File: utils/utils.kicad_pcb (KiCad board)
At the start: 2 copper layers, 32.2 x 114.5 mm, 23 parts, among them J1 AIN, J2 BIN, J3 GATE, J4 EURORACK_CONN_16, J5 ~OUT, J6 OUT, J7 Conn_01x04, J8 Conn_01x05, U1 TL072, U2 4066, U3 LM317, U4 LM337

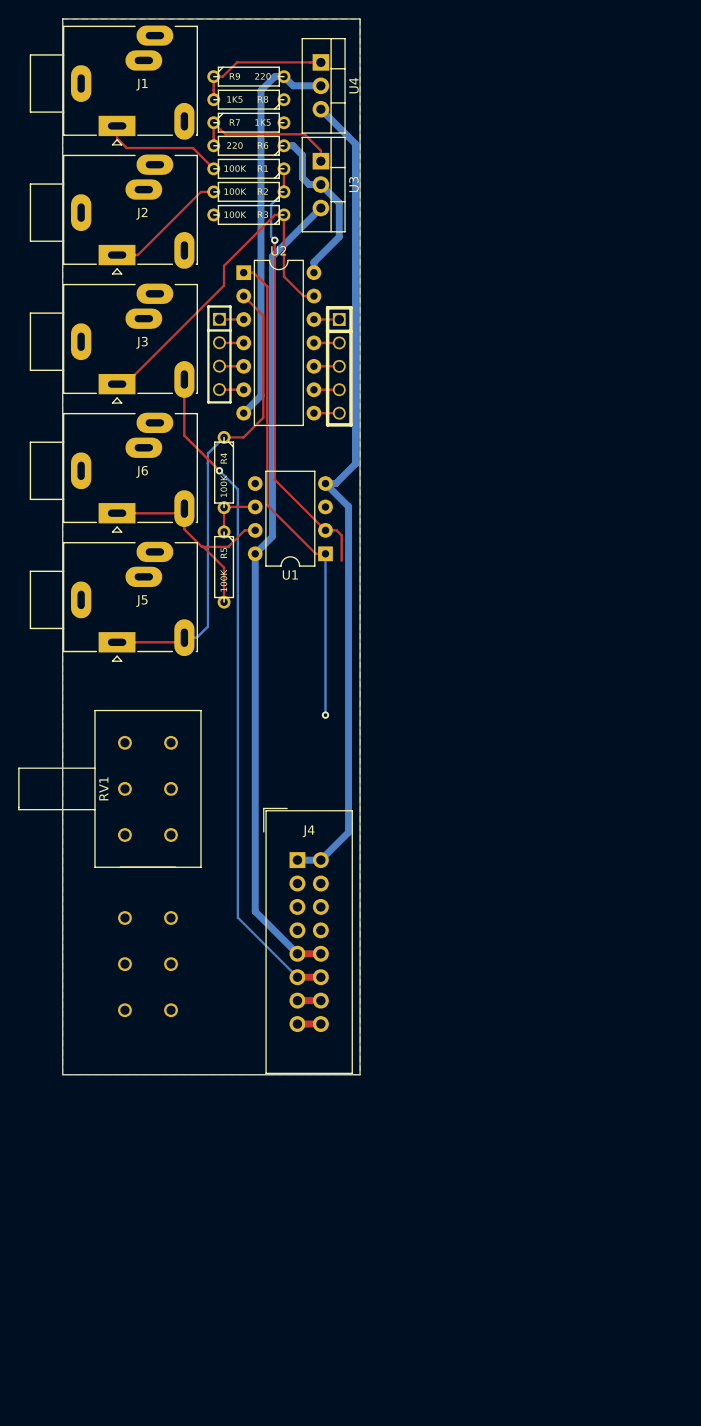
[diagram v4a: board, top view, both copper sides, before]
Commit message: shrunk board
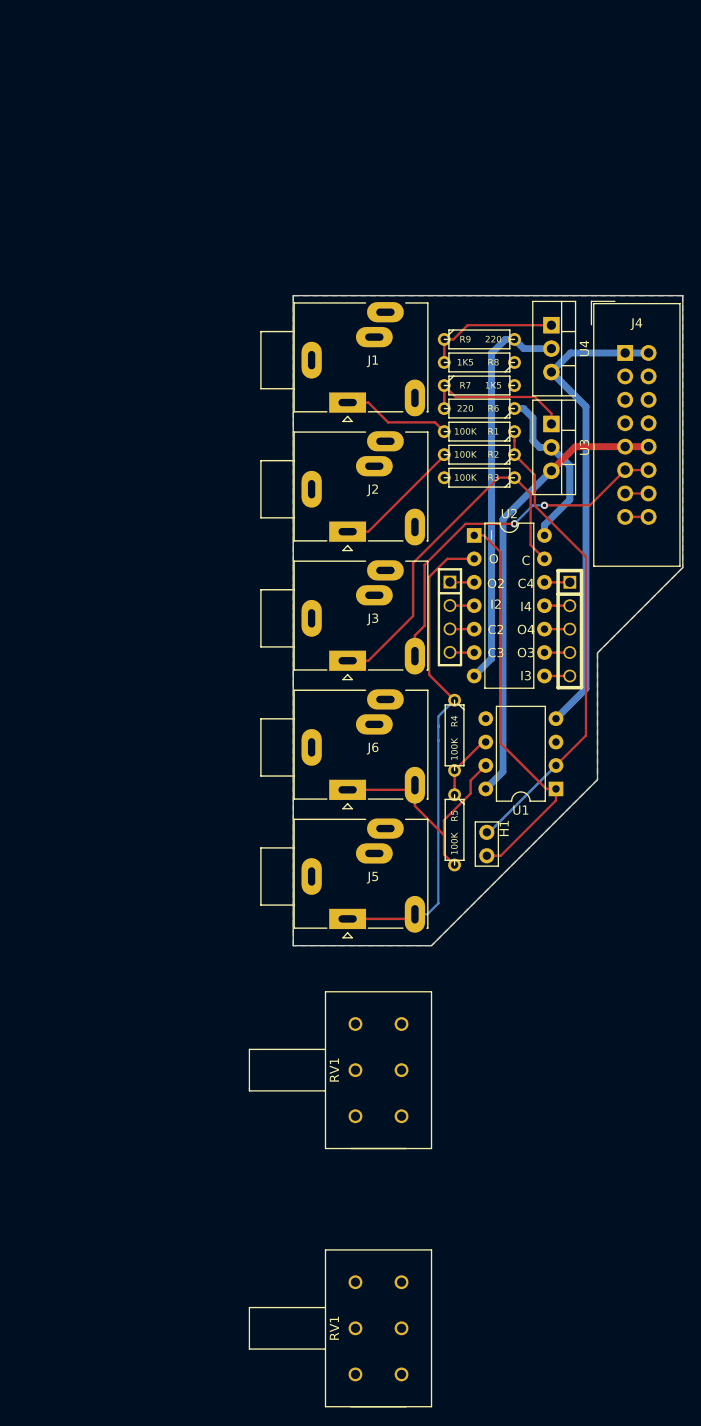
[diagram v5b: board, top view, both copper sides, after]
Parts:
- added H1: ?, 4ms/4ms-kicad-lib/lib-footprints/4ms_Connector.pretty:Pins_1x02_2.54mm_TH, F.Cu at (144.0, 102.5)
- RV1: moved to F.Cu
- moved J4 65.5 mm to (159.0, 49.2)
- moved RV1 46.7 mm to (132.2, 155.0), turned to 270 degrees
- moved RV1 39.4 mm to (132.2, 127.0)
- moved J1 39.1 mm to (128.9, 54.6)
- moved J5 39.1 mm to (128.9, 110.6)
- moved J6 39.1 mm to (128.9, 96.6)
- moved J2 39.1 mm to (128.9, 68.6)
- moved J3 39.1 mm to (128.9, 82.6)
- moved U2 37.9 mm to (142.6, 69.0)
- moved J7 37.9 mm to (140.0, 77.9)
- moved J8 37.9 mm to (153.0, 79.2)
- moved R1 37.9 mm to (143.2, 57.8)
- moved R2 37.9 mm to (143.2, 60.2)
- moved R3 37.9 mm to (143.2, 62.8)
- moved R4 37.9 mm to (140.5, 90.7)
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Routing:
- net +12V: track 88.3 -> 49.1 mm
- net -12V: track 89.8 -> 51.9 mm
- net +5V: track 72.4 -> 38.9 mm
- net Net-(RV1-Pad6): track 52.9 -> 44.0 mm, vias 1 -> 0
- net Net-(R1-Pad1): track 47.0 -> 51.3 mm, vias 1 -> 0
- net GATE: track 37.8 -> 40.7 mm
- net ~OUT: track 51.1 -> 53.6 mm
- net AIN: track 13.2 -> 11.8 mm
- net Net-(R4-Pad2): track 6.45 -> 7.81 mm
- net OUT: track 26.1 -> 27.4 mm
- net BIN: track 13.3 -> 14.0 mm
- added copper zone on B.Cu, net GND
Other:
- board size 32.2 x 114.5 mm -> 42.2 x 70.5 mm
- board text added: "BIGASS | Rev. A | 2020-05-23"
- board text added: "C"
- board text added: "C2"
- board text added: "C3"
- board text added: "C4"
- board text added: "I"
- board text added: "I2"
- board text added: "I3"
- board text added: "I4"
- board text added: "O"
- board text added: "O2"
- board text added: "O3"
- board text added: "O4"
- board text added: "https://rabid.audio"
- board text removed: "TODO: what is standard spacing for knobs?"

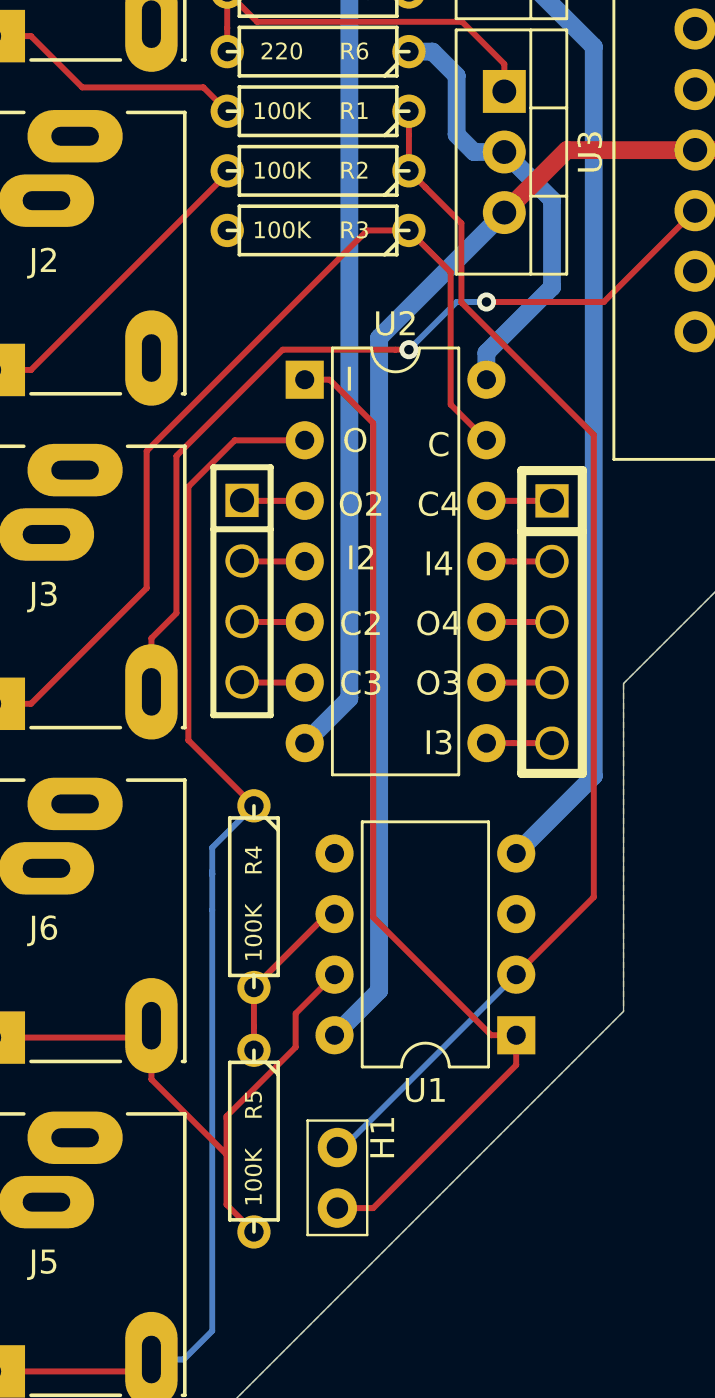
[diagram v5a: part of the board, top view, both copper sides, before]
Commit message: move the quirks of the pcb out of the schematic
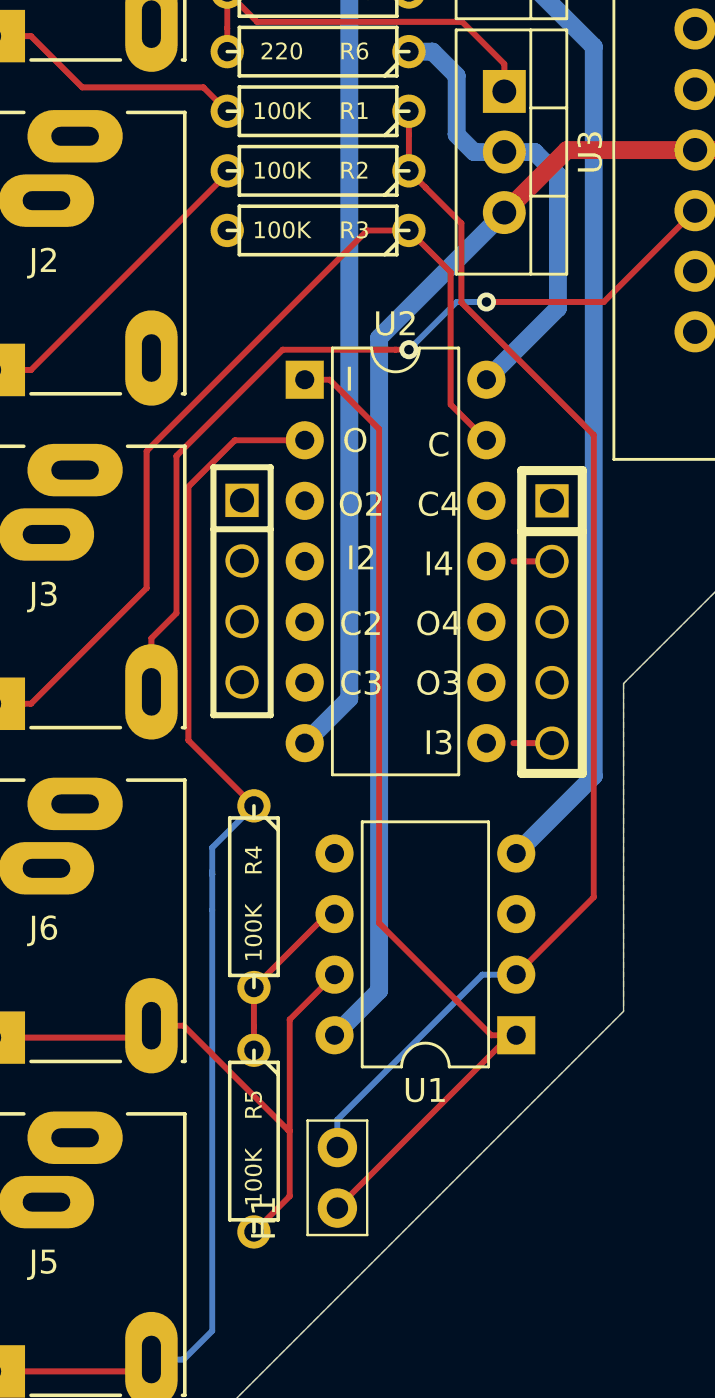
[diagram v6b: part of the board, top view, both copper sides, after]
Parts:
- RV1 (x2): value 100K -> 200K
- U3: value LM317 -> LM317L_TO92
- U4: value LM337 -> LM337L_TO92
- turned H1 to 180 degrees
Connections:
- H1 pad 1: Net-(R1-Pad1) -> Net-(RV1-Pad1)
- H1 pad 2: Net-(RV1-Pad6) -> Net-(R1-Pad1)
- RV1 pad 1: Net-(R1-Pad1) -> Net-(RV1-Pad1) (x2)
- RV1 pad 3: Net-(RV1-Pad3) -> Net-(R1-Pad1) (x2)
- RV1 pad 4: Net-(RV1-Pad3) -> (no net) (x2)
- RV1 pad 5: Net-(RV1-Pad3) -> (no net) (x2)
- RV1 pad 6: Net-(RV1-Pad6) -> (no net) (x2)
- U1 pad 1: Net-(RV1-Pad6) -> Net-(RV1-Pad1)
- U2 pad 1: Net-(RV1-Pad6) -> Net-(RV1-Pad1)
- U2 pad 10: 4066_10 -> (no net)
- U2 pad 11: 4066_11 -> (no net)
- U2 pad 12: 4066_12 -> (no net)
- U2 pad 3: 4066_3 -> (no net)
- U2 pad 4: 4066_4 -> (no net)
- U2 pad 5: 4066_5 -> (no net)
- U2 pad 6: 4066_6 -> (no net)
- U2 pad 8: 4066_8 -> (no net)
- U2 pad 9: 4066_9 -> (no net)
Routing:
- net Net-(RV1-Pad6): track 44.0 -> 0.00 mm
- net Net-(RV1-Pad1): track 0.00 -> 42.9 mm
- net 4066_9: track 2.75 -> 0.00 mm
- net 4066_12: track 2.75 -> 0.00 mm
- net 4066_10: track 2.75 -> 0.00 mm
- net 4066_6: track 2.64 -> 0.03 mm
- net 4066_5: track 2.64 -> 0.03 mm
- net 4066_4: track 2.64 -> 0.03 mm
- net 4066_3: track 2.64 -> 0.03 mm
- net 4066_8: track 2.75 -> 1.62 mm
- net 4066_11: track 2.75 -> 1.62 mm
- net Net-(R6-Pad1): track 18.7 -> 19.7 mm
- net Net-(R1-Pad1): track 51.3 -> 52.2 mm

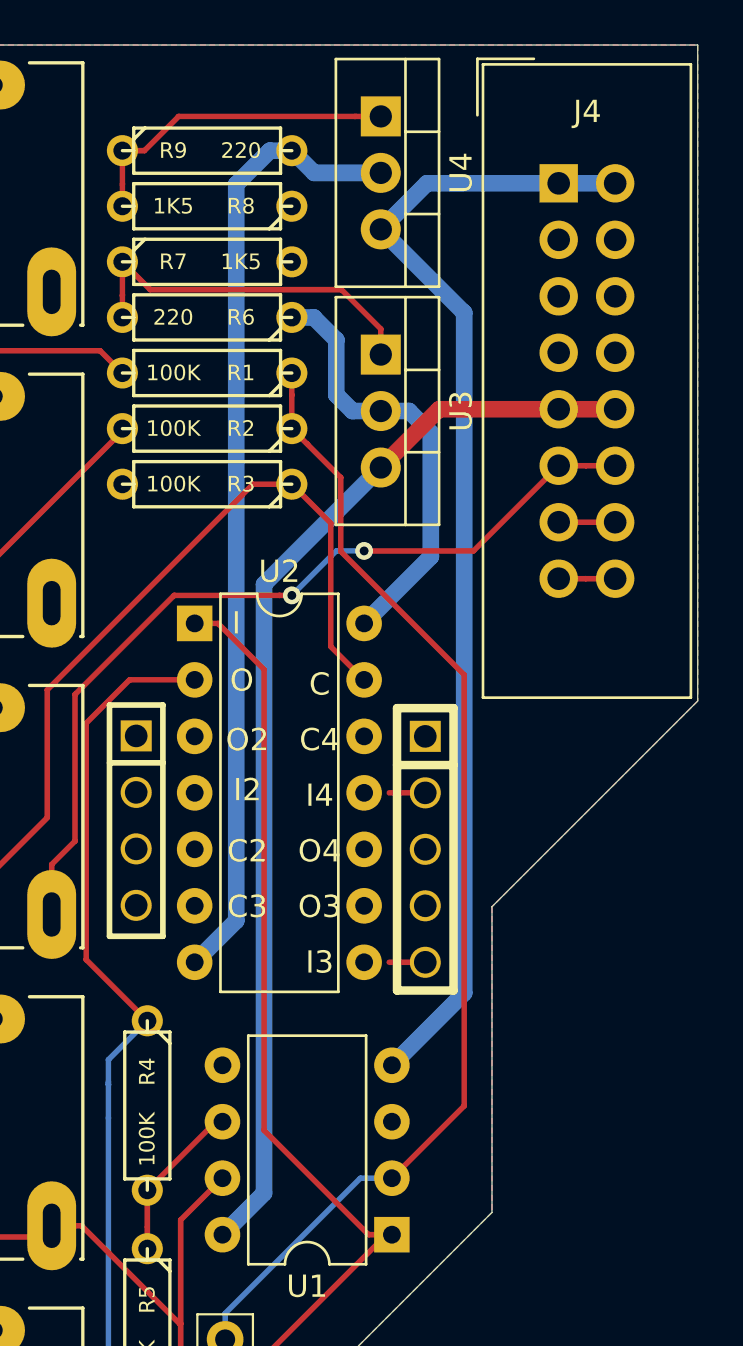
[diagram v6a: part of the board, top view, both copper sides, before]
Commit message: switch to 10-pin header
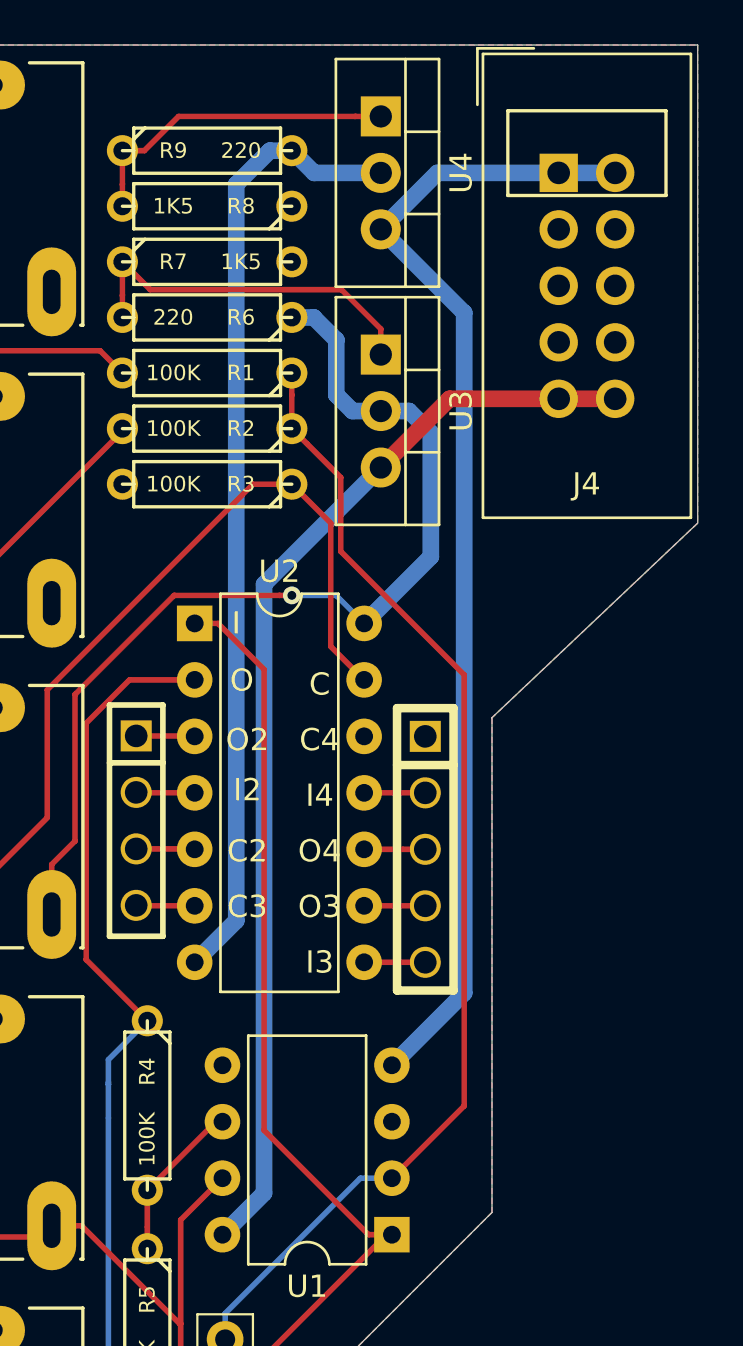
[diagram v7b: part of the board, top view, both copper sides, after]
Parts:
- J4: value EURORACK_CONN_16 -> EURORACK_CONN_10; footprint synth:EURORACK_16_IDC -> synth:EURORACK_10_IDC
- moved J4 0.47 mm to (159.0, 48.8)
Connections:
- J3 pad TN: +5V -> 7V
- R6 pad 1: Net-(R6-Pad1) -> 7V
- U2 pad 10: (no net) -> 4066_10
- U2 pad 11: (no net) -> 4066_11
- U2 pad 14: Net-(R6-Pad1) -> 7V
- U2 pad 3: (no net) -> 4066_3
- U2 pad 4: (no net) -> 4066_4
- U2 pad 5: (no net) -> 4066_5
- U2 pad 6: (no net) -> 4066_6
- U2 pad 8: (no net) -> 4066_8
- U2 pad 9: (no net) -> 4066_9
- U3 pad 2: Net-(R6-Pad1) -> 7V
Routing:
- net 7V: track 0.00 -> 45.4 mm, vias 0 -> 1
- net +5V: track 38.9 -> 0.00 mm, vias 2 -> 0
- net Net-(R6-Pad1): track 19.7 -> 0.00 mm
- net 4066_9: track 0.00 -> 2.75 mm
- net 4066_10: track 0.00 -> 2.75 mm
- net 4066_3: track 0.03 -> 2.67 mm
- net 4066_5: track 0.03 -> 2.67 mm
- net 4066_6: track 0.03 -> 2.64 mm
- net 4066_4: track 0.03 -> 2.64 mm
- net Net-(J4-Pad15): track 2.54 -> 0.00 mm
- net Net-(J4-Pad13): track 2.54 -> 0.00 mm
- net 4066_8: track 1.62 -> 2.75 mm
- net 4066_11: track 1.62 -> 2.75 mm
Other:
- outline, holes or cut-outs redrawn
- board text removed: "TODO: what’s the orientation of this?"

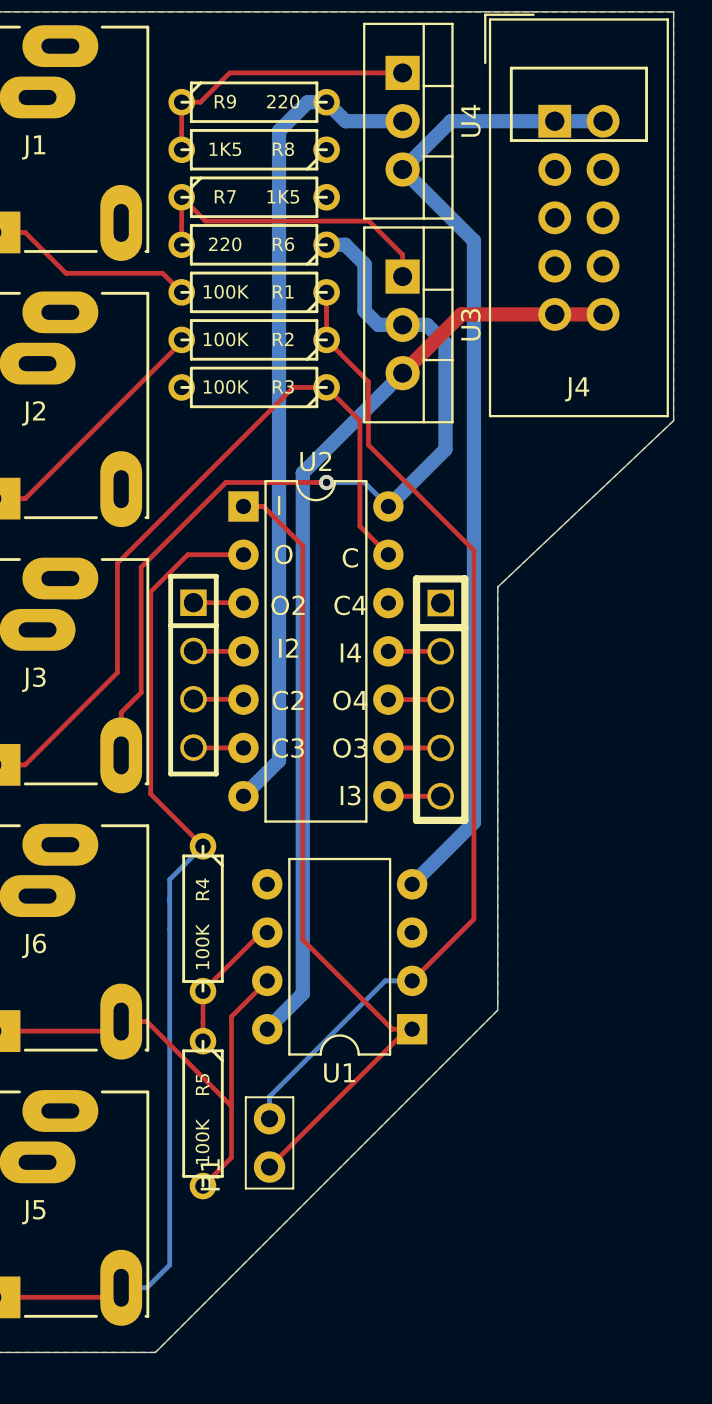
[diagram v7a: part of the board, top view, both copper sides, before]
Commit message: use +/-10V power supply for amps
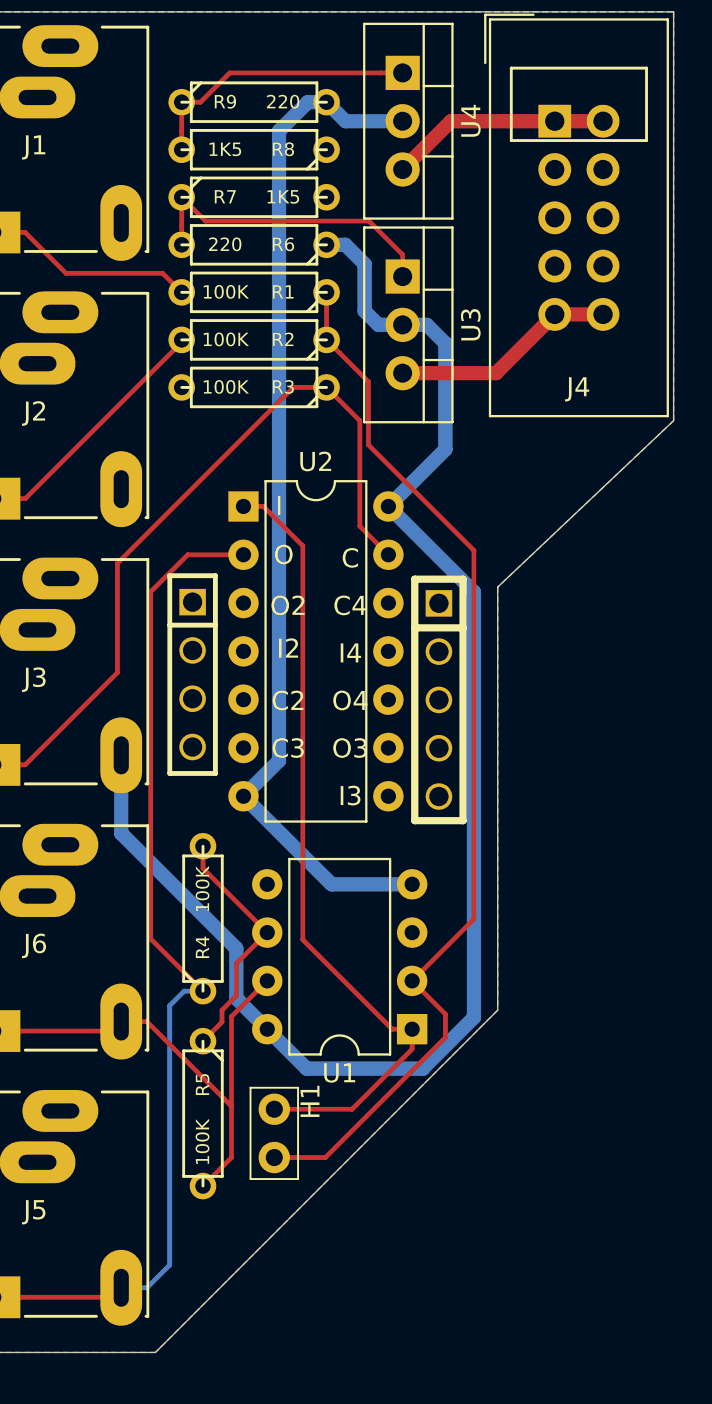
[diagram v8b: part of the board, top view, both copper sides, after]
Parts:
- moved H1 0.56 mm to (144.2, 102.0), turned to 0 degrees
- moved J8 0.09 mm to (152.9, 79.2)
- moved J7 0.05 mm to (140.0, 77.9)
- turned R4 to 90 degrees
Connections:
- J3 pad TN: 7V -> +10V
- J4 pad 1: -12V -> Net-(J4-Pad1)
- J4 pad 9: +12V -> Net-(J4-Pad9)
- J7 pad 1: 4066_3 -> (no net)
- J7 pad 2: 4066_4 -> (no net)
- J7 pad 3: 4066_5 -> (no net)
- J7 pad 4: 4066_6 -> (no net)
- J8 pad 1: 4066_12 -> (no net)
- J8 pad 2: 4066_11 -> (no net)
- J8 pad 3: 4066_10 -> (no net)
- J8 pad 4: 4066_9 -> (no net)
- J8 pad 5: 4066_8 -> (no net)
- R3 pad 2: GND -> -10V
- R6 pad 1: 7V -> +10V
- R9 pad 2: Net-(R9-Pad2) -> -10V
- U1 pad 4: -12V -> -10V
- U1 pad 8: +12V -> +10V
- U2 pad 10: 4066_10 -> (no net)
- U2 pad 11: 4066_11 -> (no net)
- U2 pad 14: 7V -> +10V
- U2 pad 3: 4066_3 -> (no net)
- U2 pad 4: 4066_4 -> (no net)
- U2 pad 5: 4066_5 -> (no net)
- U2 pad 6: 4066_6 -> (no net)
- U2 pad 7: Net-(R9-Pad2) -> -10V
- U2 pad 8: 4066_8 -> (no net)
- U2 pad 9: 4066_9 -> (no net)
- U3 pad 2: 7V -> +10V
- U3 pad 3: +12V -> Net-(J4-Pad9)
- U4 pad 2: Net-(R9-Pad2) -> -10V
- U4 pad 3: -12V -> Net-(J4-Pad1)
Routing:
- net +10V: track 0.00 -> 78.8 mm
- net -10V: track 0.00 -> 54.6 mm
- net -12V: track 52.1 -> 0.00 mm
- net +12V: track 49.3 -> 0.00 mm
- net 7V: track 45.4 -> 0.00 mm, vias 1 -> 0
- net Net-(R9-Pad2): track 43.8 -> 0.00 mm
- net Net-(J4-Pad9): track 0.00 -> 11.8 mm
- net Net-(J4-Pad1): track 0.00 -> 11.6 mm
- net Net-(R4-Pad2): track 7.81 -> 13.8 mm
- net Net-(R1-Pad1): track 52.2 -> 56.1 mm
- net 4066_9: track 2.75 -> 0.00 mm
- net 4066_8: track 2.75 -> 0.00 mm
- net 4066_11: track 2.75 -> 0.00 mm
- net 4066_10: track 2.75 -> 0.00 mm
- net 4066_3: track 2.67 -> 0.00 mm
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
